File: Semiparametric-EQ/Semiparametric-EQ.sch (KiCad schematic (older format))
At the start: 11 parts, among them U1 NE5532

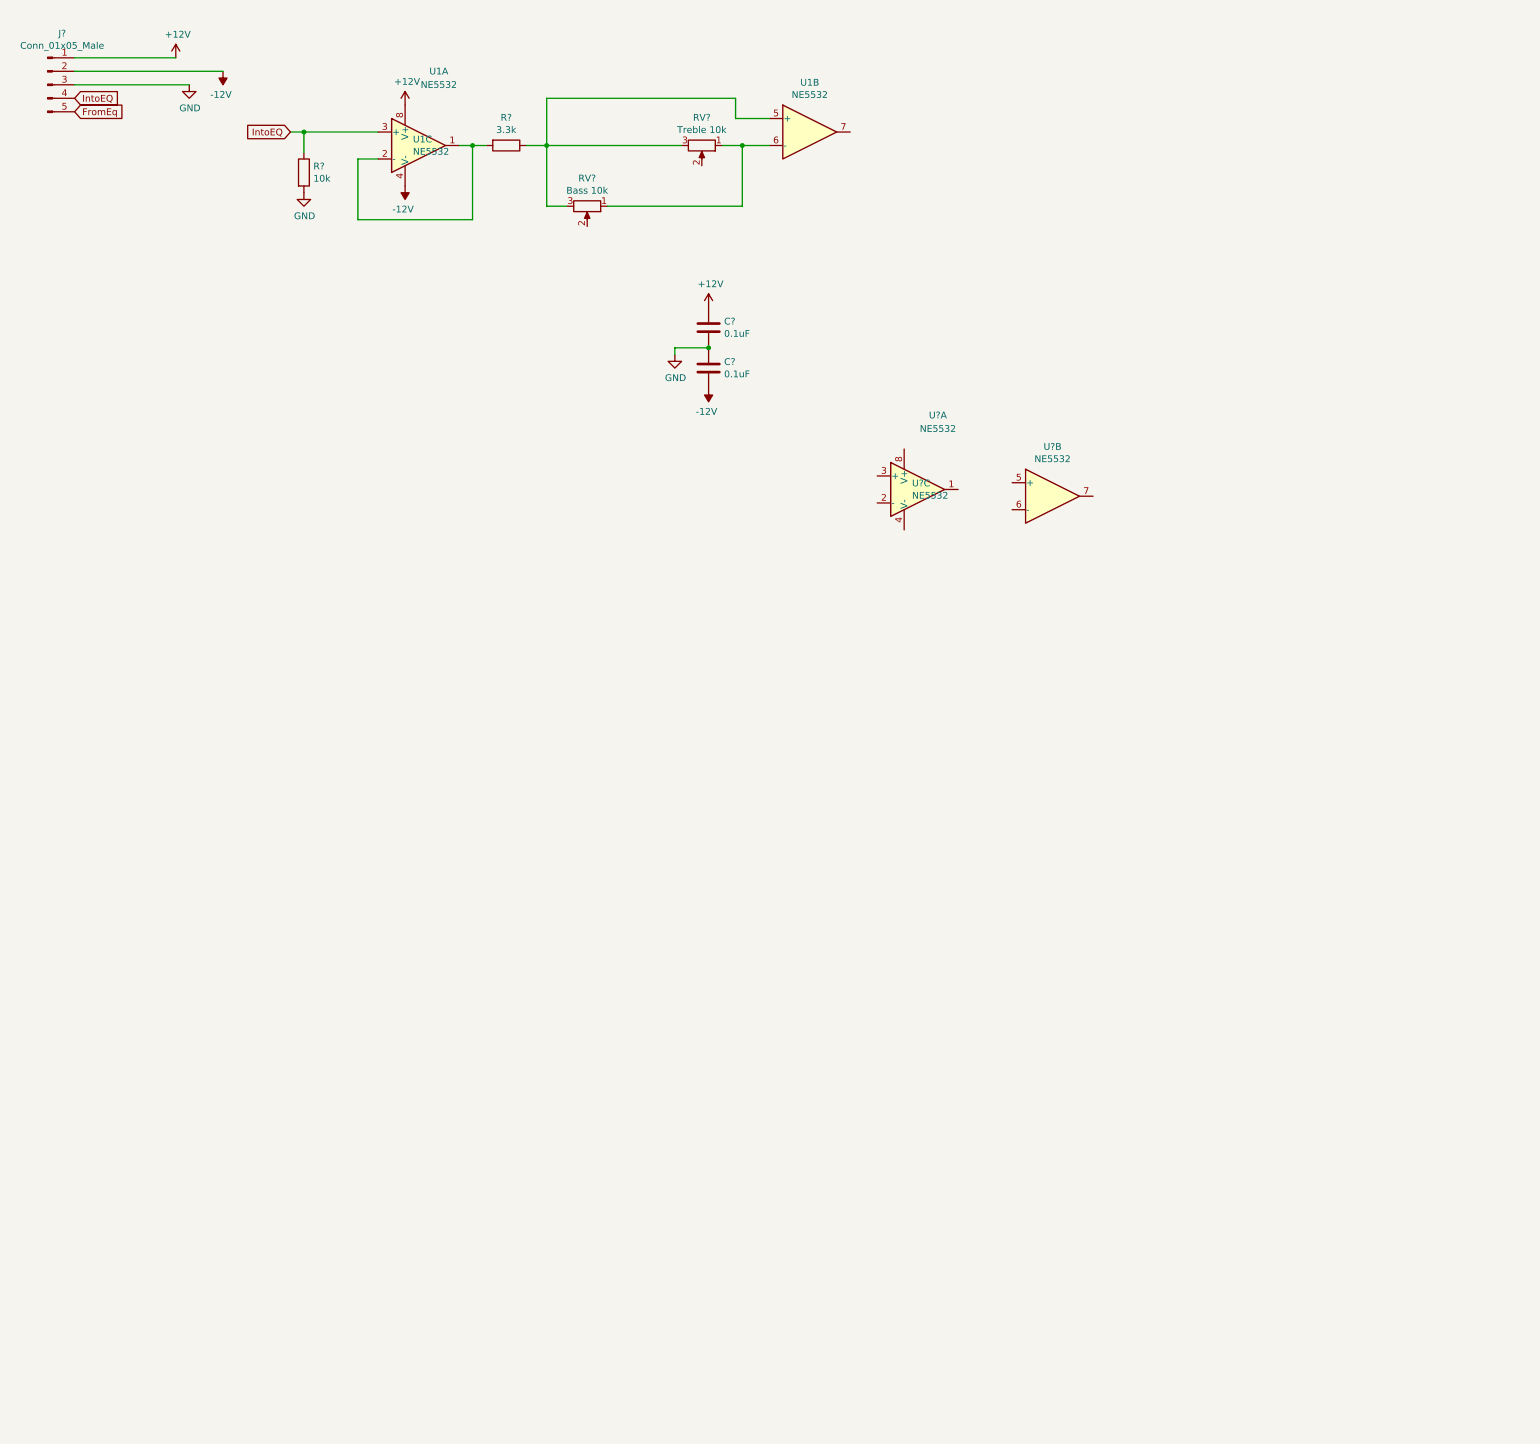
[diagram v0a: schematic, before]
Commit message: Added bulk caps, started eq board layout
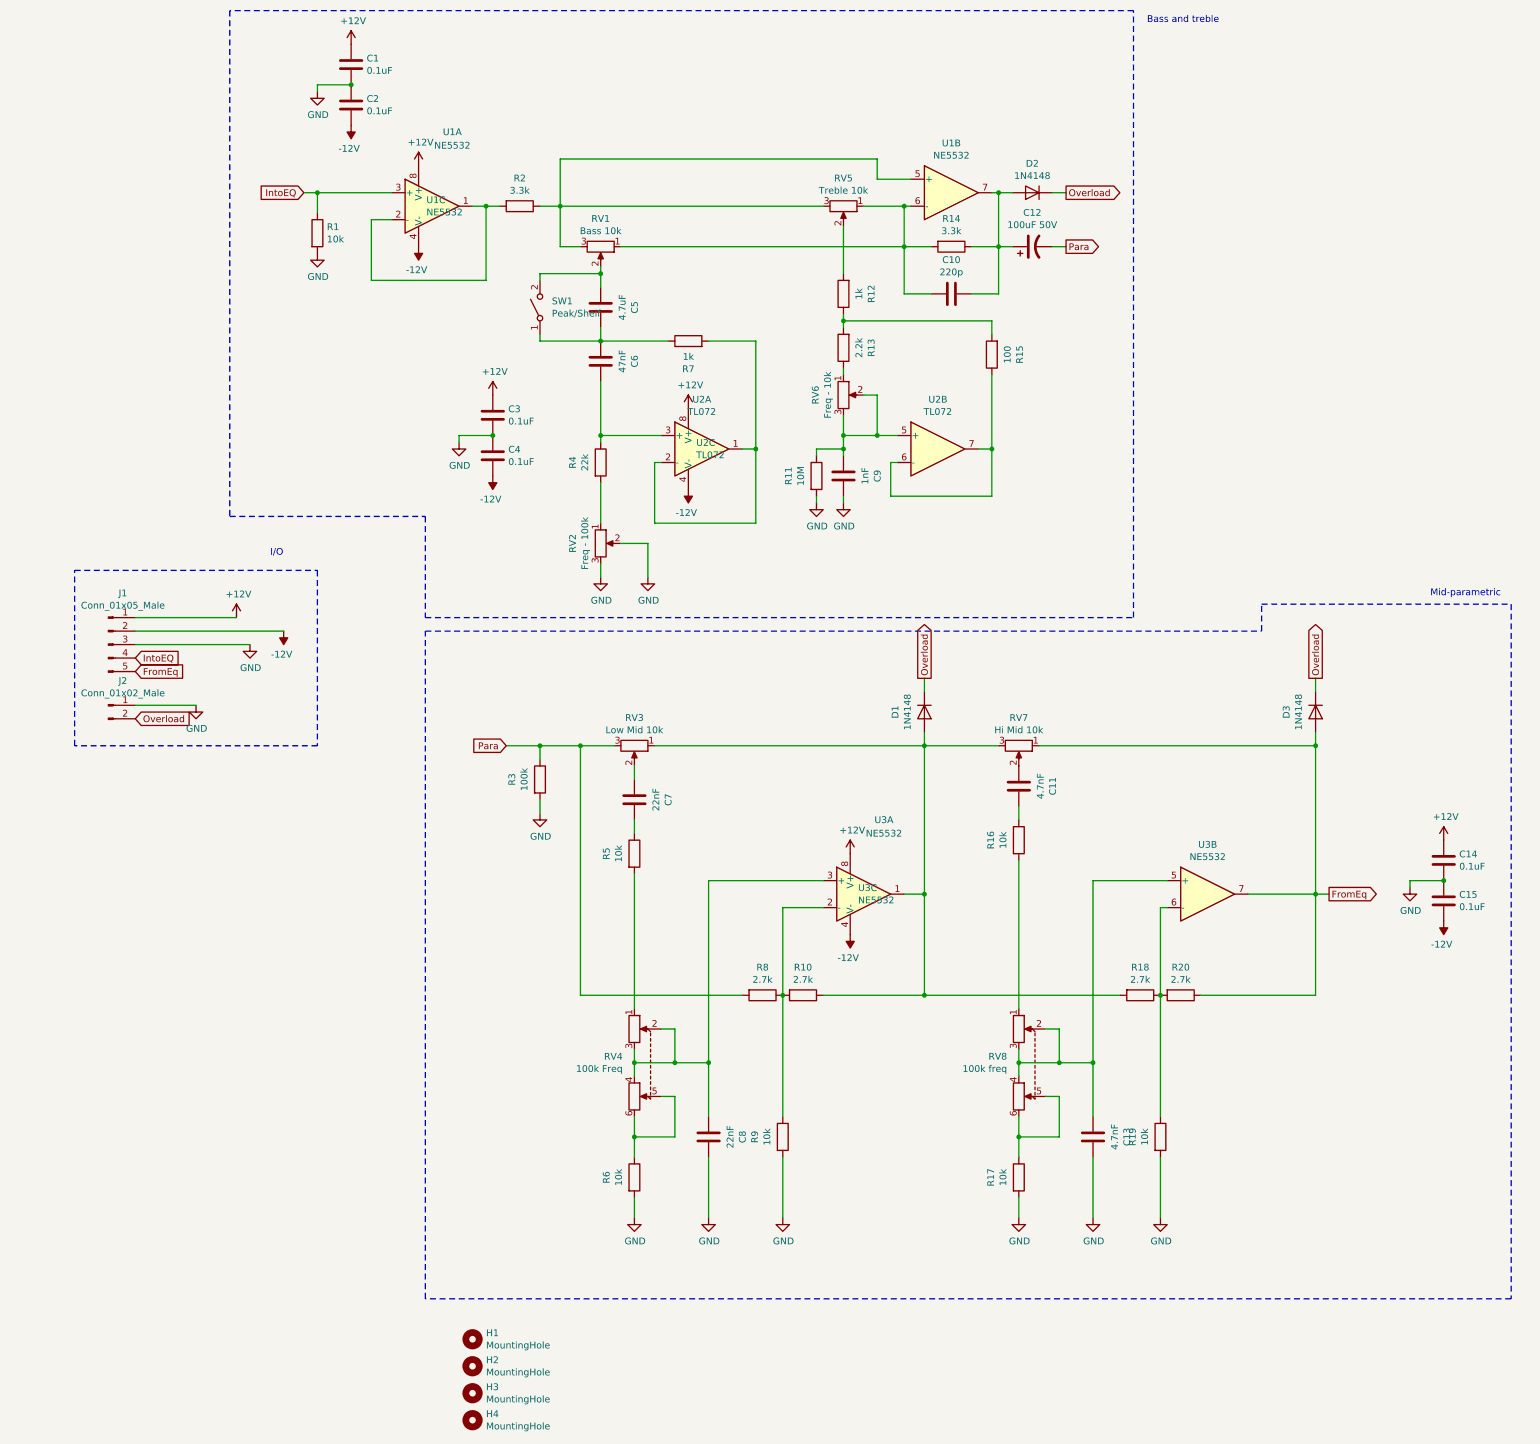
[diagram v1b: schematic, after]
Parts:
- added C10: 220p, Capacitor_SMD:C_0805_2012Metric_Pad1.15x1.40mm_HandSolder, symbol Device:C
- added C11, C13: 4.7nF, Capacitor_SMD:C_0805_2012Metric_Pad1.15x1.40mm_HandSolder, symbol Device:C
- added C12: 100uF 50V, Capacitor_THT:CP_Radial_D8.0mm_P3.50mm, symbol Device:CP1
- added C14, C15, C3, C4: 0.1uF, Capacitor_SMD:C_0805_2012Metric_Pad1.15x1.40mm_HandSolder, symbol Device:C
- added C5: 4.7uF, Capacitor_THT:C_Rect_L7.2mm_W8.5mm_P5.00mm_FKP2_FKP2_MKS2_MKP2, symbol Device:C
- added C6: 47nF, Capacitor_SMD:C_0805_2012Metric_Pad1.15x1.40mm_HandSolder, symbol Device:C
- added C7, C8: 22nF, Capacitor_SMD:C_0805_2012Metric_Pad1.15x1.40mm_HandSolder, symbol Device:C
- added C9: 1nF, Capacitor_SMD:C_0805_2012Metric_Pad1.15x1.40mm_HandSolder, symbol Device:C
- added D1, D2, D3: 1N4148, Diode_THT:D_DO-35_SOD27_P7.62mm_Horizontal, symbol Diode:1N4148
- added H1, H2, H3, H4: MountingHole, MountingHole:MountingHole_3.2mm_M3_ISO7380, symbol Mechanical:MountingHole
- added J2: Conn_01x02_Male, Connector_PinHeader_2.54mm:PinHeader_1x02_P2.54mm_Vertical, symbol Connector:Conn_01x02_Male
- added R10, R18, R20, R8: 2.7k, Resistor_SMD:R_0805_2012Metric_Pad1.15x1.40mm_HandSolder, symbol Device:R
- added R11: 10M, Resistor_SMD:R_0805_2012Metric_Pad1.15x1.40mm_HandSolder, symbol Device:R
- added R12, R7: 1k, Resistor_SMD:R_0805_2012Metric_Pad1.15x1.40mm_HandSolder, symbol Device:R
- added R13: 2.2k, Resistor_SMD:R_0805_2012Metric_Pad1.15x1.40mm_HandSolder, symbol Device:R
- added R14: 3.3k, Resistor_SMD:R_0805_2012Metric_Pad1.15x1.40mm_HandSolder, symbol Device:R
- added R15: 100, Resistor_SMD:R_0805_2012Metric_Pad1.15x1.40mm_HandSolder, symbol Device:R
- added R16, R17, R19, R5, R6, R9: 10k, Resistor_SMD:R_0805_2012Metric_Pad1.15x1.40mm_HandSolder, symbol Device:R
- added R3: 100k, Resistor_SMD:R_0805_2012Metric_Pad1.15x1.40mm_HandSolder, symbol Device:R
- added R4: 22k, Resistor_SMD:R_0805_2012Metric_Pad1.15x1.40mm_HandSolder, symbol Device:R
- added RV2: Freq - 100k, Connector_PinHeader_2.54mm:PinHeader_1x03_P2.54mm_Vertical, symbol Device:R_POT
- added RV3: Low Mid 10k, Connector_PinHeader_2.54mm:PinHeader_1x03_P2.54mm_Vertical, symbol Device:R_POT
- added RV4: 100k Freq, Connector_PinHeader_2.54mm:PinHeader_1x06_P2.54mm_Vertical, symbol Device:R_POT_Dual
- added RV6: Freq - 10k, Connector_PinHeader_2.54mm:PinHeader_1x03_P2.54mm_Vertical, symbol Device:R_POT
- added RV7: Hi Mid 10k, Connector_PinHeader_2.54mm:PinHeader_1x03_P2.54mm_Vertical, symbol Device:R_POT
- added RV8: 100k freq, Connector_PinHeader_2.54mm:PinHeader_1x06_P2.54mm_Vertical, symbol Device:R_POT_Dual
- added SW1: Peak/Shelf, Connector_PinHeader_2.54mm:PinHeader_1x02_P2.54mm_Vertical, symbol Switch:SW_SPST
- added U2: TL072, Package_DIP:DIP-8_W7.62mm_Socket, symbol Amplifier_Operational:TL072
- C1, C2: renamed from C?; footprint (none) -> Capacitor_SMD:C_0805_2012Metric_Pad1.15x1.40mm_HandSolder
- J1: renamed from J?; footprint (none) -> Connector_PinHeader_2.54mm:PinHeader_1x05_P2.54mm_Vertical
- R1, R2: renamed from R?; footprint (none) -> Resistor_SMD:R_0805_2012Metric_Pad1.15x1.40mm_HandSolder
- RV1, RV5: renamed from RV?; footprint (none) -> Connector_PinHeader_2.54mm:PinHeader_1x03_P2.54mm_Vertical
- U1: footprint (none) -> Package_DIP:DIP-8_W7.62mm_Socket
- U3: renamed from U?; footprint (none) -> Package_DIP:DIP-8_W7.62mm_Socket
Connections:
- net +12V: now also U3.8 (V+), C14.1, C3.1, U2.8 (V+)
- net -12V: now also U3.4 (V-), C15.2, C4.2, U2.4 (V-)
- net FromEq: now also U3.7, D3.2 (A), R20.1, RV7.1
- net GND: now also C13.1, C14.2, C15.1, C3.2, C4.1, C8.1, C9.1, J2.1 (Pin_1), R11.2, R17.2, R19.2, R3.2, R6.2, R9.2, RV2.2, RV2.3
- net at RV1.1, RV5.1, U1.6 (-): now also C10.2, R14.2
- net at U1.7: now also C10.1, C12.1, D2.2 (A), R14.1
- net at U3.1: now also D1.2 (A), R10.1, R18.2, RV3.1, RV7.3
- net at U3.2 (-): now also R10.2, R8.1, R9.1
- net at U3.3 (+): now also C8.2, RV4.2, RV4.3, RV4.4
- net at U3.5 (+): now also C13.2, RV8.2, RV8.3, RV8.4
- net at U3.6 (-): now also R18.1, R19.1, R20.2
- net at RV5.2: now also R12.2
- net at RV1.2: now also C5.2, SW1.2 (B)
- new net: R12.1, R13.2, R15.2
- new net: C5.1, C6.2, R7.1, SW1.1 (A)
- new net: R7.2, U2.1, U2.2 (-)
- new net: C6.1, R4.1, U2.3 (+)
- new net: C9.2, R11.1, RV6.2, RV6.3, U2.5 (+)
- new net: R15.1, U2.6 (-), U2.7
- new net: R4.2, RV2.1
- new net: R13.1, RV6.1
- new net: C7.2, RV3.2
- new net: C7.1, R5.1
- new net: R5.2, RV4.1
- new net: R6.1, RV4.5, RV4.6
- new net: C11.2, RV7.2
- new net: C11.1, R16.1
- new net: R16.2, RV8.1
- new net: R17.1, RV8.5, RV8.6
- new net Overload: D1.1 (K), D2.1 (K), D3.1 (K), J2.2 (Pin_2)
- new net Para: C12.2, R3.1, R8.2, RV3.3
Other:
- note added: "Bass and treble"
- note added: "I/O"
- note added: "Mid-parametric"
- moved on the sheet: C1, C2, J1, R1, R2, RV1, RV5, U1A, U1B, U1C, U3A, U3B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

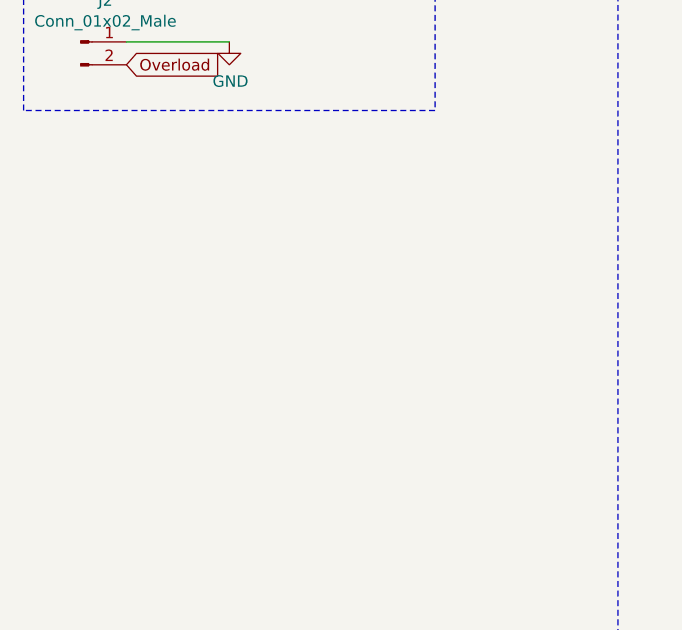
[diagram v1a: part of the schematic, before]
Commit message: More layout work on the EQ unit
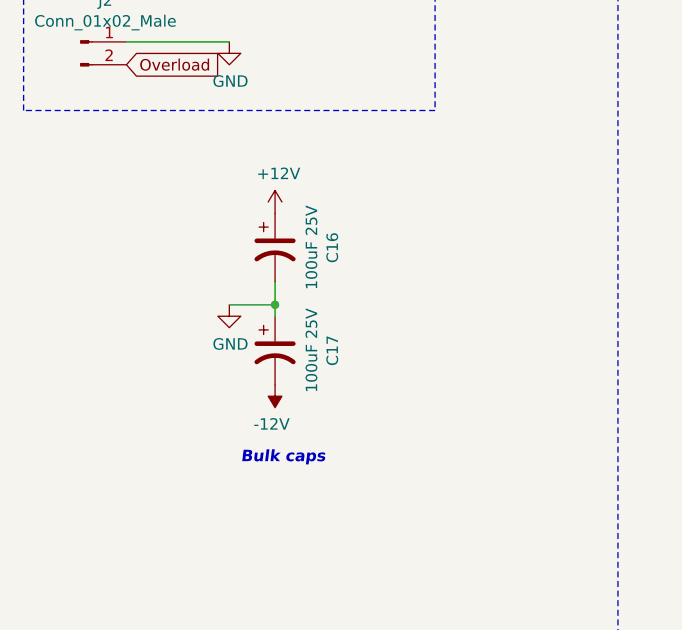
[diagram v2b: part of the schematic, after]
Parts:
- added C16, C17: 100uF 25V, Capacitor_THT:CP_Radial_D6.3mm_P2.50mm, symbol Device:CP1
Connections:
- net +12V: now also C16.1
- net -12V: now also C17.2
- net GND: now also C16.2, C17.1
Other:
- note added: "Bulk caps"
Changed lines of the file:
@@
 	1    0    0    -1
 $EndComp
+$Comp
+L Device:CP1 C16
+U 1 1 5E75B6D5
+P 2500 6700
+F 0 "C16" V 2752 6700 50  0000 C CNN
+F 1 "100uF 25V" V 2661 6700 50  0000 C CNN
+F 2 "Capacitor_THT:CP_Radial_D6.3mm_P2.50mm" H 2500 6700 50  0001 C CNN
+F 3 "~" H 2500 6700 50  0001 C CNN
+	1    2500 6700
+	1    0    0    -1
+$EndComp
+$Comp
+L Device:CP1 C17
+U 1 1 5E75BB94
+P 2500 7150
+F 0 "C17" V 2752 7150 50  0000 C CNN
+F 1 "100uF 25V" V 2661 7150 50  0000 C CNN
+F 2 "Capacitor_THT:CP_Radial_D6.3mm_P2.50mm" H 2500 7150 50  0001 C CNN
+F 3 "~" H 2500 7150 50  0001 C CNN
+	1    2500 7150
+	1    0    0    -1
+$EndComp
+$Comp
+L power:+12V #PWR0132
+U 1 1 5E76B515
+P 2500 6550
+F 0 "#PWR0132" H 2500 6400 50  0001 C CNN
+F 1 "+12V" H 2515 6723 50  0000 C CNN
+F 2 "" H 2500 6550 50  0001 C CNN
+F 3 "" H 2500 6550 50  0001 C CNN
+	1    2500 6550
+	1    0    0    -1
+$EndComp
+$Comp
+L power:-12V #PWR0133
+U 1 1 5E76B8E6
+P 2500 7300
+F 0 "#PWR0133" H 2500 7400 50  0001 C CNN
+F 1 "-12V" H 2515 7473 50  0000 C CNN
+F 2 "" H 2500 7300 50  0001 C CNN
+F 3 "" H 2500 7300 50  0001 C CNN
+	1    2500 7300
+	-1   0    0    1
+$EndComp
+$Comp
+L power:GND #PWR0134
+U 1 1 5E76BC84
+P 2300 6950
+F 0 "#PWR0134" H 2300 6700 50  0001 C CNN
+F 1 "GND" H 2305 6777 50  0000 C CNN
+F 2 "" H 2300 6950 50  0001 C CNN
+F 3 "" H 2300 6950 50  0001 C CNN
+	1    2300 6950
+	1    0    0    -1
+$EndComp
+Wire Wire Line
+	2500 6950 2300 6950
+Wire Wire Line
+	2500 6850 2500 6950
+Connection ~ 2500 6950
+Wire Wire Line
+	2500 6950 2500 7000
+Text Notes 2350 7650 0    50   Italic 10
+Bulk caps
 $EndSCHEMATC

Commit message: Finished first pass at Eq board
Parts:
- removed C3, C4: 0.1uF, Capacitor_SMD:C_0805_2012Metric_Pad1.15x1.40mm_HandSolder, symbol Device:C
- added C18, C19: 0.1uF, Capacitor_SMD:C_0805_2012Metric_Pad1.15x1.40mm_HandSolder, symbol Device:C
- D1, D2, D3: footprint Diode_THT:D_DO-35_SOD27_P7.62mm_Horizontal -> Diode_SMD:D_SOD-123
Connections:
- net +12V: now also C18.1
- net -12V: now also C19.2
- net GND: now also C18.2, C19.1
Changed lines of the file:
@@
 F 0 "D2" H 8500 1784 50  0000 C CNN
 F 1 "1N4148" H 8500 1875 50  0000 C CNN
-F 2 "Diode_THT:D_DO-35_SOD27_P7.62mm_Horizontal" H 8500 1825 50  0001 C CNN
+F 2 "Diode_SMD:D_SOD-123" H 8500 1825 50  0001 C CNN
 F 3 "https://assets.nexperia.com/documents/data-sheet/1N4148_1N4448.pdf" H 8500 2000 50  0001 C CNN
 	1    8500 2000
@@
 $EndComp
 $Comp
-L power:GND #PWR0111
-U 1 1 5E4C6F25
-P 4250 3850
-F 0 "#PWR0111" H 4250 3600 50  0001 C CNN
-F 1 "GND" H 4255 3677 50  0000 C CNN
-F 2 "" H 4250 3850 50  0001 C CNN
-F 3 "" H 4250 3850 50  0001 C CNN
-	1    4250 3850
-	1    0    0    -1
-$EndComp
-$Comp
-L power:+12V #PWR0112
-U 1 1 5E4C6F2B
-P 4500 3500
-F 0 "#PWR0112" H 4500 3350 50  0001 C CNN
-F 1 "+12V" H 4515 3673 50  0000 C CNN
-F 2 "" H 4500 3500 50  0001 C CNN
-F 3 "" H 4500 3500 50  0001 C CNN
-	1    4500 3500
-	1    0    0    -1
-$EndComp
-$Comp
-L power:-12V #PWR0113
-U 1 1 5E4C6F31
-P 4500 4100
-F 0 "#PWR0113" H 4500 4200 50  0001 C CNN
-F 1 "-12V" H 4515 4273 50  0000 C CNN
-F 2 "" H 4500 4100 50  0001 C CNN
-F 3 "" H 4500 4100 50  0001 C CNN
-	1    4500 4100
-	-1   0    0    1
-$EndComp
-$Comp
-L Device:C C3
-U 1 1 5E4C6F37
-P 4500 3650
-F 0 "C3" H 4615 3696 50  0000 L CNN
-F 1 "0.1uF" H 4615 3605 50  0000 L CNN
-F 2 "Capacitor_SMD:C_0805_2012Metric_Pad1.15x1.40mm_HandSolder" H 4538 3500 50  0001 C CNN
-F 3 "~" H 4500 3650 50  0001 C CNN
-	1    4500 3650
-	1    0    0    -1
-$EndComp
-$Comp
-L Device:C C4
-U 1 1 5E4C6F3D
-P 4500 3950
-F 0 "C4" H 4615 3996 50  0000 L CNN
-F 1 "0.1uF" H 4615 3905 50  0000 L CNN
-F 2 "Capacitor_SMD:C_0805_2012Metric_Pad1.15x1.40mm_HandSolder" H 4538 3800 50  0001 C CNN
-F 3 "~" H 4500 3950 50  0001 C CNN
-	1    4500 3950
-	1    0    0    -1
-$EndComp
-Wire Wire Line
-	4500 3800 4250 3800
-Wire Wire Line
-	4250 3800 4250 3850
-Connection ~ 4500 3800
-$Comp
 L power:+12V #PWR0114
 U 1 1 5E4C79A7
@@
 F 0 "D1" H 7700 5634 50  0000 C CNN
 F 1 "1N4148" H 7700 5725 50  0000 C CNN
-F 2 "Diode_THT:D_DO-35_SOD27_P7.62mm_Horizontal" H 7700 5675 50  0001 C CNN
+F 2 "Diode_SMD:D_SOD-123" H 7700 5675 50  0001 C CNN
 F 3 "https://assets.nexperia.com/documents/data-sheet/1N4148_1N4448.pdf" H 7700 5850 50  0001 C CNN
 	1    7700 5850
@@
 F 0 "D3" H 10600 5634 50  0000 C CNN
 F 1 "1N4148" H 10600 5725 50  0000 C CNN
-F 2 "Diode_THT:D_DO-35_SOD27_P7.62mm_Horizontal" H 10600 5675 50  0001 C CNN
+F 2 "Diode_SMD:D_SOD-123" H 10600 5675 50  0001 C CNN
 F 3 "https://assets.nexperia.com/documents/data-sheet/1N4148_1N4448.pdf" H 10600 5850 50  0001 C CNN
 	1    10600 5850
@@
 Text Notes 2350 7650 0    50   Italic 10
 Bulk caps
+$Comp
+L power:GND #PWR01
+U 1 1 5E980DCF
+P 8650 3400
+F 0 "#PWR01" H 8650 3150 50  0001 C CNN
+F 1 "GND" H 8655 3227 50  0000 C CNN
+F 2 "" H 8650 3400 50  0001 C CNN
+F 3 "" H 8650 3400 50  0001 C CNN
+	1    8650 3400
+	1    0    0    -1
+$EndComp
+$Comp
+L power:+12V #PWR02
+U 1 1 5E980DD5
+P 8900 3050
+F 0 "#PWR02" H 8900 2900 50  0001 C CNN
+F 1 "+12V" H 8915 3223 50  0000 C CNN
+F 2 "" H 8900 3050 50  0001 C CNN
+F 3 "" H 8900 3050 50  0001 C CNN
+	1    8900 3050
+	1    0    0    -1
+$EndComp
+$Comp
+L power:-12V #PWR03
+U 1 1 5E980DDB
+P 8900 3650
+F 0 "#PWR03" H 8900 3750 50  0001 C CNN
+F 1 "-12V" H 8915 3823 50  0000 C CNN
+F 2 "" H 8900 3650 50  0001 C CNN
+F 3 "" H 8900 3650 50  0001 C CNN
+	1    8900 3650
+	-1   0    0    1
+$EndComp
+$Comp
+L Device:C C18
+U 1 1 5E980DE1
+P 8900 3200
+F 0 "C18" H 9015 3246 50  0000 L CNN
+F 1 "0.1uF" H 9015 3155 50  0000 L CNN
+F 2 "Capacitor_SMD:C_0805_2012Metric_Pad1.15x1.40mm_HandSolder" H 8938 3050 50  0001 C CNN
+F 3 "~" H 8900 3200 50  0001 C CNN
+	1    8900 3200
+	1    0    0    -1
+$EndComp
+$Comp
+L Device:C C19
+U 1 1 5E980DE7
+P 8900 3500
+F 0 "C19" H 9015 3546 50  0000 L CNN
+F 1 "0.1uF" H 9015 3455 50  0000 L CNN
+F 2 "Capacitor_SMD:C_0805_2012Metric_Pad1.15x1.40mm_HandSolder" H 8938 3350 50  0001 C CNN
+F 3 "~" H 8900 3500 50  0001 C CNN
+	1    8900 3500
+	1    0    0    -1
+$EndComp
+Wire Wire Line
+	8900 3350 8650 3350
+Wire Wire Line
+	8650 3350 8650 3400
+Connection ~ 8900 3350
 $EndSCHEMATC
